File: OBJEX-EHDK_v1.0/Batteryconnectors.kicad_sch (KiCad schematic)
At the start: 15 parts

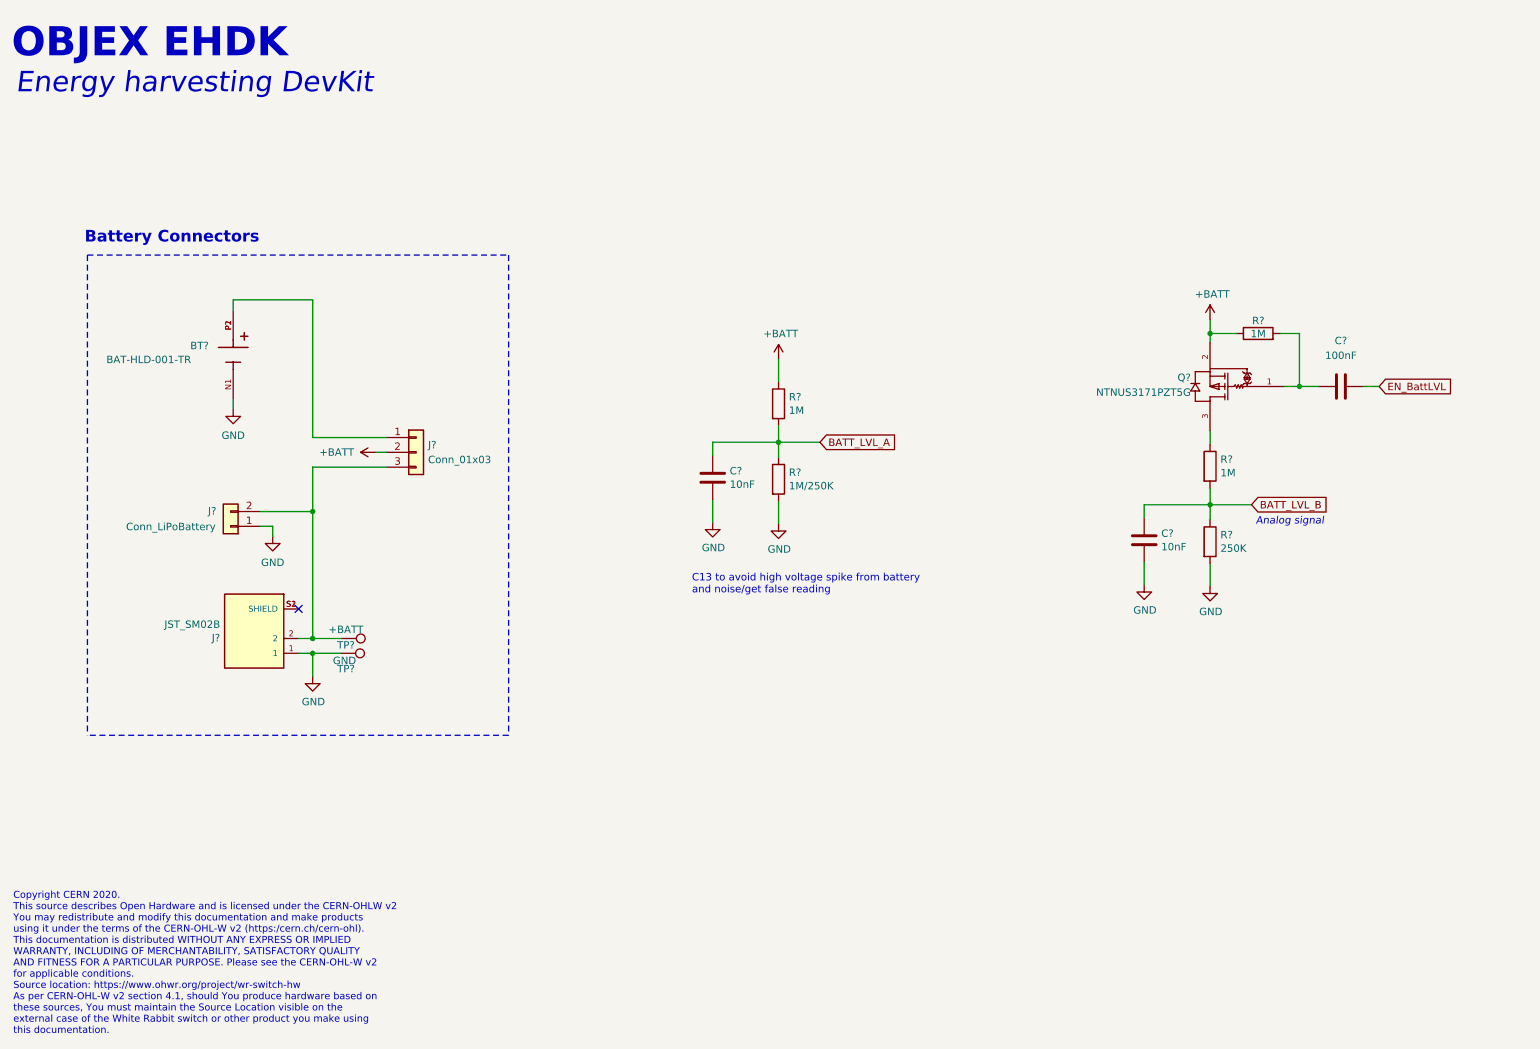
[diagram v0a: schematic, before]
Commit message: add: nRF52840 & SPV1050TTR
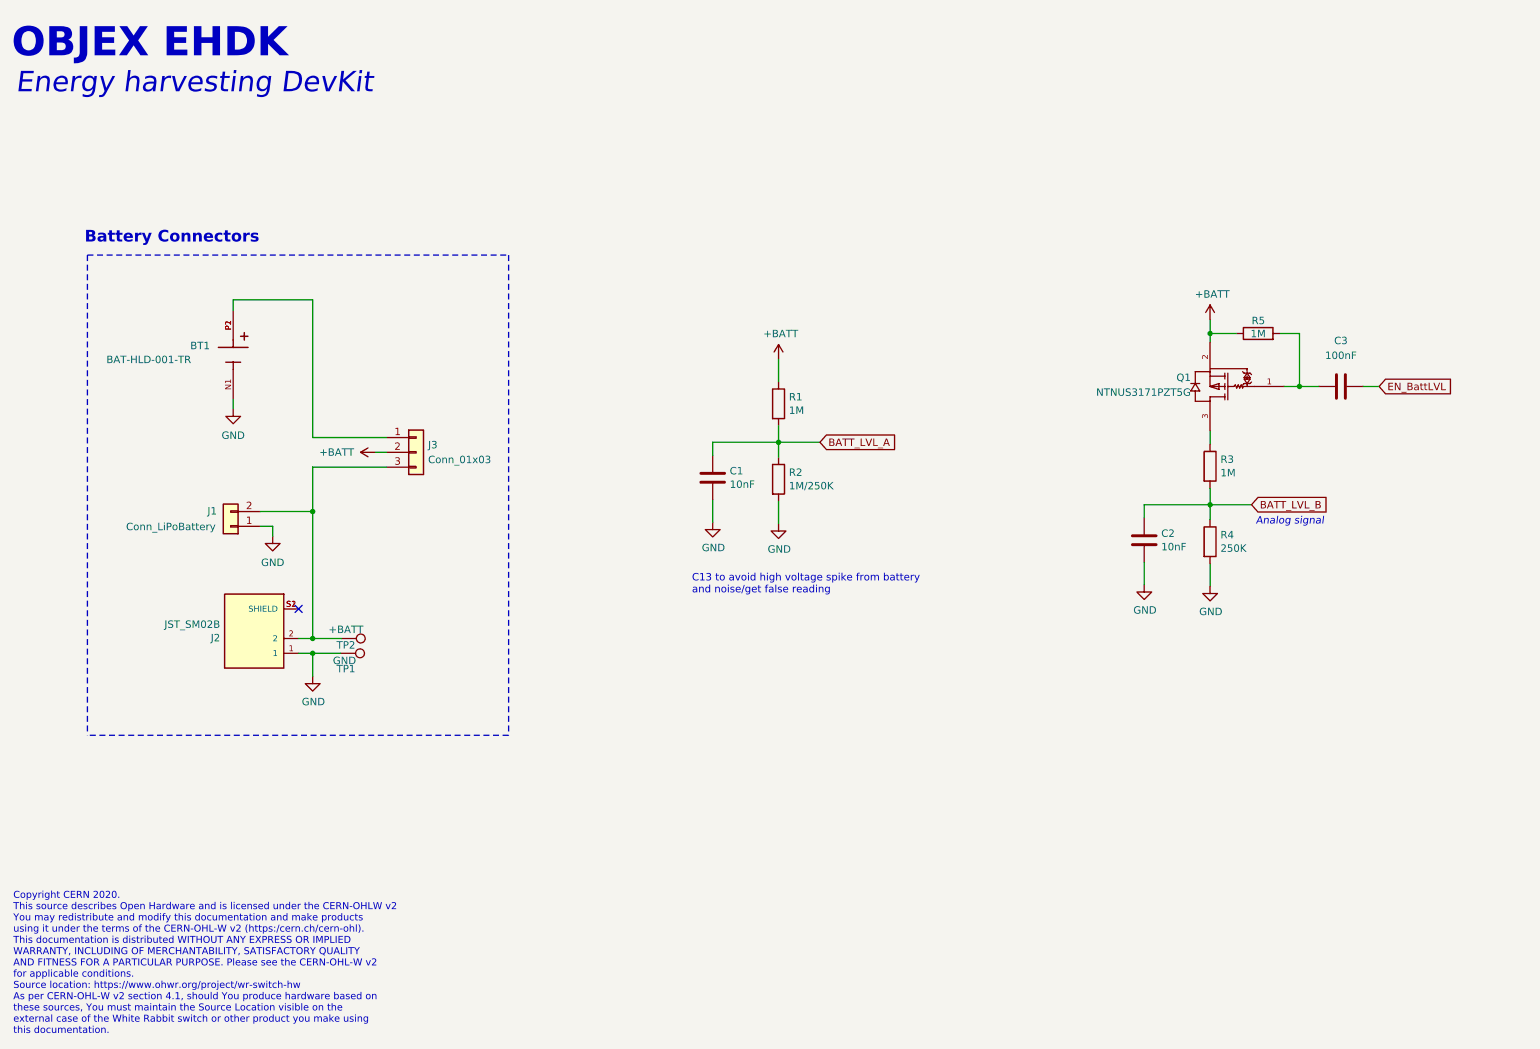
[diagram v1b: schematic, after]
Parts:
- gave numbers to parts that had none: 15
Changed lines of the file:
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@@
   (symbol (lib_id "power:GND") (at 70.3834 132.2832 0) (unit 1)
     (in_bom yes) (on_board yes)
-    (property "Reference" "#PWR?" (id 0) (at 70.3834 138.6332 0)
+    (property "Reference" "#PWR0102" (id 0) (at 70.3834 138.6332 0)
       (effects (font (size 1.27 1.27)) hide)
     )
@@
   (symbol (lib_id "power:GND") (at 150.3426 106.0958 0) (unit 1)
     (in_bom yes) (on_board yes)
-    (property "Reference" "#PWR?" (id 0) (at 150.3426 112.4458 0)
+    (property "Reference" "#PWR0108" (id 0) (at 150.3426 112.4458 0)
       (effects (font (size 1.27 1.27)) hide)
     )
@@
   (symbol (lib_id "Connector:TestPoint") (at 75.3364 125.8062 270) (unit 1)
     (in_bom yes) (on_board yes)
-    (property "Reference" "TP?" (id 0) (at 76.0984 126.9492 90))
+    (property "Reference" "TP2" (id 0) (at 76.0984 126.9492 90))
     (property "Value" "+BATT" (id 1) (at 76.0984 124.2822 90))
     (property "Footprint" "TestPoint:TestPoint_Pad_1.5x1.5mm" (id 2) (at 75.3364 130.8862 0)
@@
   (symbol (lib_id "Device:C") (at 246.8626 82.55 90) (unit 1)
     (in_bom yes) (on_board yes) (fields_autoplaced)
-    (property "Reference" "C?" (id 0) (at 246.8626 74.7014 90))
+    (property "Reference" "C3" (id 0) (at 246.8626 74.7014 90))
     (property "Value" "100nF" (id 1) (at 246.8626 77.2414 90))
     (property "Footprint" "Capacitor_SMD:C_0402_1005Metric" (id 2) (at 250.6726 81.5848 0)
@@
   (symbol (lib_id "Device:R") (at 232.664 73.4568 90) (unit 1)
     (in_bom yes) (on_board yes)
-    (property "Reference" "R?" (id 0) (at 232.6894 71.2724 90))
+    (property "Reference" "R5" (id 0) (at 232.6894 71.2724 90))
     (property "Value" "1M" (id 1) (at 232.664 73.5076 90))
     (property "Footprint" "Resistor_SMD:R_0402_1005Metric" (id 2) (at 232.664 75.2348 90)
@@
   (symbol (lib_id "Device:C") (at 139.0396 98.2218 0) (unit 1)
     (in_bom yes) (on_board yes)
-    (property "Reference" "C?" (id 0) (at 141.9606 97.0534 0)
+    (property "Reference" "C1" (id 0) (at 141.9606 97.0534 0)
       (effects (font (size 1.27 1.27)) (justify left))
     )
@@
   (symbol (lib_id "Device:C") (at 213.106 108.9406 0) (unit 1)
     (in_bom yes) (on_board yes)
-    (property "Reference" "C?" (id 0) (at 216.027 107.7722 0)
+    (property "Reference" "C2" (id 0) (at 216.027 107.7722 0)
       (effects (font (size 1.27 1.27)) (justify left))
     )
@@
   (symbol (lib_id "Device:R") (at 224.409 96.2406 0) (unit 1)
     (in_bom yes) (on_board yes)
-    (property "Reference" "R?" (id 0) (at 226.187 95.0722 0)
+    (property "Reference" "R3" (id 0) (at 226.187 95.0722 0)
       (effects (font (size 1.27 1.27)) (justify left))
     )
@@
   (symbol (lib_id "Connector_Generic:Conn_01x02") (at 56.3118 106.553 180) (unit 1)
     (in_bom yes) (on_board yes)
-    (property "Reference" "J?" (id 0) (at 53.1368 103.9368 0))
+    (property "Reference" "J1" (id 0) (at 53.1368 103.9368 0))
     (property "Value" "Conn_LiPoBattery" (id 1) (at 46.0502 106.6292 0))
     (property "Footprint" "" (id 2) (at 56.3118 106.553 0)
@@
   (symbol (lib_id "NTNUS3171PZT5G:NTNUS3171PZT5G") (at 232.029 85.09 180) (unit 1)
     (in_bom yes) (on_board yes) (fields_autoplaced)
-    (property "Reference" "Q?" (id 0) (at 221.107 81.0259 0)
+    (property "Reference" "Q1" (id 0) (at 221.107 81.0259 0)
       (effects (font (size 1.27 1.27)) (justify left))
     )
@@
   (symbol (lib_id "Device:R") (at 150.3426 98.4758 0) (unit 1)
     (in_bom yes) (on_board yes)
-    (property "Reference" "R?" (id 0) (at 152.1206 97.3074 0)
+    (property "Reference" "R2" (id 0) (at 152.1206 97.3074 0)
       (effects (font (size 1.27 1.27)) (justify left))
     )
@@
   (symbol (lib_id "power:GND") (at 213.106 116.5606 0) (unit 1)
     (in_bom yes) (on_board yes)
-    (property "Reference" "#PWR?" (id 0) (at 213.106 122.9106 0)
+    (property "Reference" "#PWR0110" (id 0) (at 213.106 122.9106 0)
       (effects (font (size 1.27 1.27)) hide)
     )
@@
   (symbol (lib_id "power:+BATT") (at 150.3426 77.9018 0) (unit 1)
     (in_bom yes) (on_board yes)
-    (property "Reference" "#PWR?" (id 0) (at 150.3426 81.7118 0)
+    (property "Reference" "#PWR0106" (id 0) (at 150.3426 81.7118 0)
       (effects (font (size 1.27 1.27)) hide)
     )
@@
   (symbol (lib_id "power:GND") (at 139.0396 105.8418 0) (unit 1)
     (in_bom yes) (on_board yes)
-    (property "Reference" "#PWR?" (id 0) (at 139.0396 112.1918 0)
+    (property "Reference" "#PWR0109" (id 0) (at 139.0396 112.1918 0)
       (effects (font (size 1.27 1.27)) hide)
     )
@@
   (symbol (lib_id "BAT-HLD-001-TR:BAT-HLD-001-TR") (at 56.7436 77.1144 270) (unit 1)
     (in_bom yes) (on_board yes)
-    (property "Reference" "BT?" (id 0) (at 49.3776 75.565 90)
+    (property "Reference" "BT1" (id 0) (at 49.3776 75.565 90)
       (effects (font (size 1.27 1.27)) (justify left))
     )
@@
   (symbol (lib_id "power:+BATT") (at 81.153 93.853 90) (unit 1)
     (in_bom yes) (on_board yes) (fields_autoplaced)
-    (property "Reference" "#PWR?" (id 0) (at 84.963 93.853 0)
+    (property "Reference" "#PWR0104" (id 0) (at 84.963 93.853 0)
       (effects (font (size 1.27 1.27)) hide)
     )
@@
   (symbol (lib_id "Device:R") (at 150.3426 85.5218 0) (unit 1)
     (in_bom yes) (on_board yes)
-    (property "Reference" "R?" (id 0) (at 152.1206 84.3534 0)
+    (property "Reference" "R1" (id 0) (at 152.1206 84.3534 0)
       (effects (font (size 1.27 1.27)) (justify left))
     )
@@
   (symbol (lib_id "power:GND") (at 63.5254 108.2294 0) (unit 1)
     (in_bom yes) (on_board yes) (fields_autoplaced)
-    (property "Reference" "#PWR?" (id 0) (at 63.5254 114.5794 0)
+    (property "Reference" "#PWR0103" (id 0) (at 63.5254 114.5794 0)
       (effects (font (size 1.27 1.27)) hide)
     )
@@
   (symbol (lib_id "Device:R") (at 224.409 109.1946 0) (unit 1)
     (in_bom yes) (on_board yes)
-    (property "Reference" "R?" (id 0) (at 226.187 108.0262 0)
+    (property "Reference" "R4" (id 0) (at 226.187 108.0262 0)
       (effects (font (size 1.27 1.27)) (justify left))
     )
@@
   (symbol (lib_id "power:GND") (at 224.409 116.8146 0) (unit 1)
     (in_bom yes) (on_board yes)
-    (property "Reference" "#PWR?" (id 0) (at 224.409 123.1646 0)
+    (property "Reference" "#PWR0111" (id 0) (at 224.409 123.1646 0)
       (effects (font (size 1.27 1.27)) hide)
     )
@@
   (symbol (lib_id "SM02B-SURS-TF_LF__SN_:SM02B-SURS-TF(LF)(SN)") (at 60.3504 125.8062 180) (unit 1)
     (in_bom yes) (on_board yes)
-    (property "Reference" "J?" (id 0) (at 54.5084 125.7046 0)
+    (property "Reference" "J2" (id 0) (at 54.5084 125.7046 0)
       (effects (font (size 1.27 1.27)) (justify left))
     )
@@
   (symbol (lib_id "Connector_Generic:Conn_01x03") (at 88.138 93.853 0) (unit 1)
     (in_bom yes) (on_board yes) (fields_autoplaced)
-    (property "Reference" "J?" (id 0) (at 90.1954 92.5829 0)
+    (property "Reference" "J3" (id 0) (at 90.1954 92.5829 0)
       (effects (font (size 1.27 1.27)) (justify left))
     )
@@
   (symbol (lib_id "Connector:TestPoint") (at 75.2094 128.3462 270) (unit 1)
     (in_bom yes) (on_board yes)
-    (property "Reference" "TP?" (id 0) (at 76.0984 131.0132 90))
+    (property "Reference" "TP1" (id 0) (at 76.0984 131.0132 90))
     (property "Value" "GND" (id 1) (at 75.8444 129.6162 90))
     (property "Footprint" "TestPoint:TestPoint_Pad_1.5x1.5mm" (id 2) (at 75.2094 133.4262 0)
@@
   (symbol (lib_id "power:GND") (at 56.7436 86.4108 0) (unit 1)
     (in_bom yes) (on_board yes) (fields_autoplaced)
-    (property "Reference" "#PWR?" (id 0) (at 56.7436 92.7608 0)
+    (property "Reference" "#PWR0105" (id 0) (at 56.7436 92.7608 0)
       (effects (font (size 1.27 1.27)) hide)
     )
@@
   (symbol (lib_id "power:+BATT") (at 224.409 71.12 0) (unit 1)
     (in_bom yes) (on_board yes)
-    (property "Reference" "#PWR?" (id 0) (at 224.409 74.93 0)
-      (effects (font (size 1.27 1.27)) hide)
-    )
+    (property "Reference" "#PWR0107" (id 0) (at 224.409 74.93 0)
+      (effects (font (size 1.27 1.27)) hide)
+    )

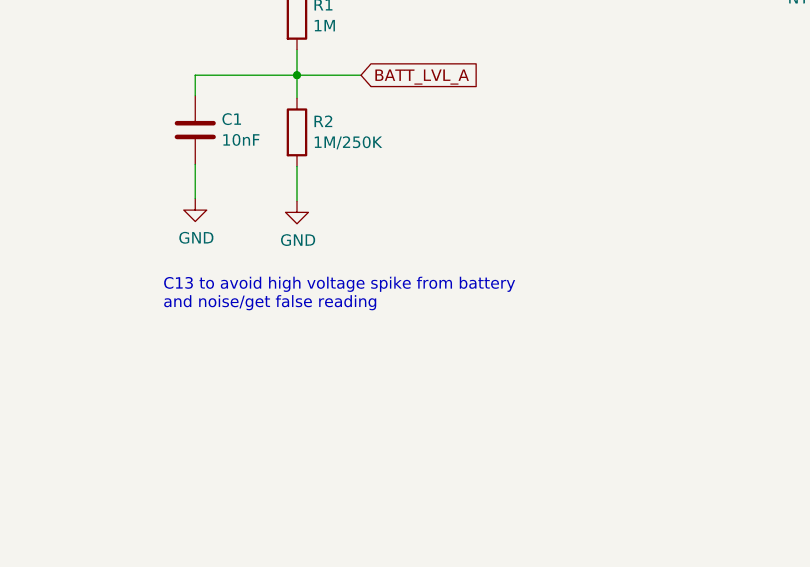
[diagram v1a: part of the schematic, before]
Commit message: add: ADP5091
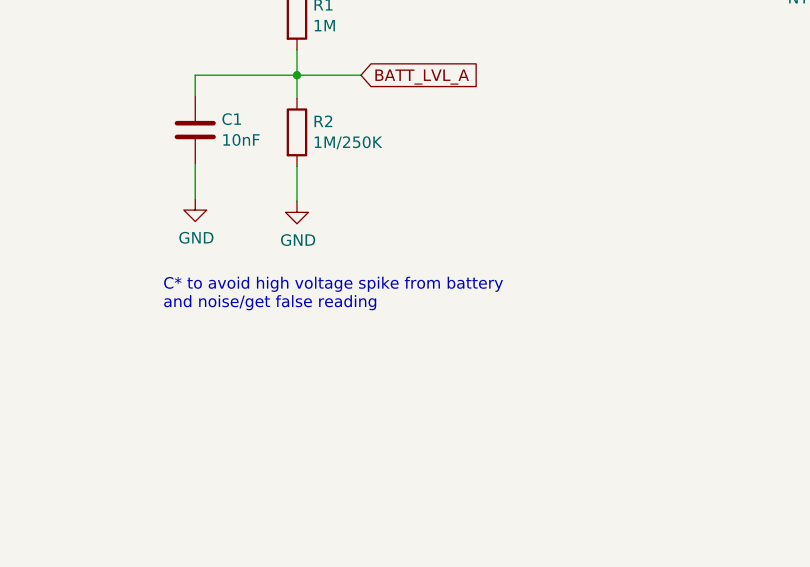
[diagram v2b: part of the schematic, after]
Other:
- note added: "C* to avoid high voltage spike from battery and noise/get false reading"
- note removed: "C13 to avoid high voltage spike from battery and noise/get false reading"
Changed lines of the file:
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@@
     (effects (font (size 5 5) (thickness 0.8) bold) (justify left bottom))
   )
-  (text "C13 to avoid high voltage spike from battery \nand noise/get false reading"
+  (text "C* to avoid high voltage spike from battery \nand noise/get false reading"
     (at 135.4836 118.2878 0)
     (effects (font (size 1.27 1.27)) (justify left bottom))
